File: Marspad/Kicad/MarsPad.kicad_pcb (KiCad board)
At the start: 2 copper layers, 81.5 x 83.2 mm, 30 parts, among them J1 OLED_128x64, SW1 RotaryEncoder_Switch, SW2 RotaryEncoder_Switch, U2 RP2040_Zero

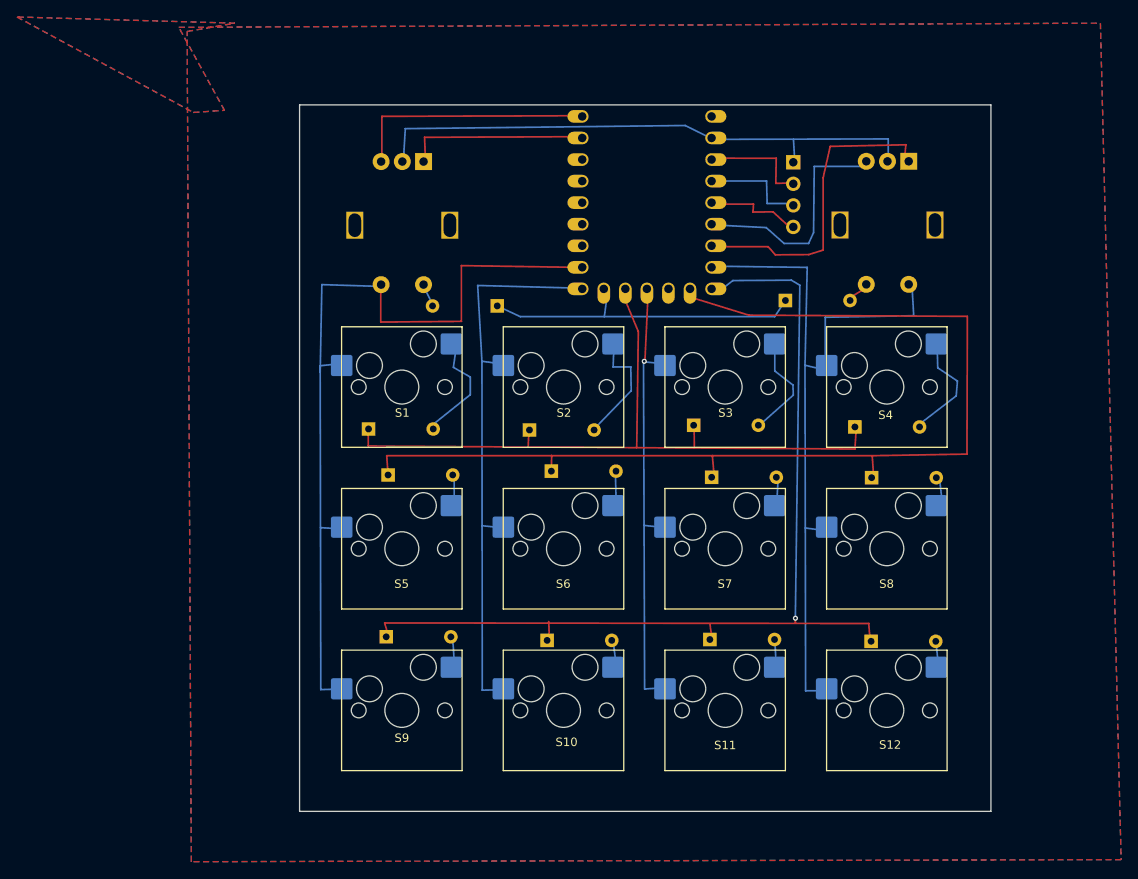
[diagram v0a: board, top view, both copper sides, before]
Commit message: added header for WS2812 led strips
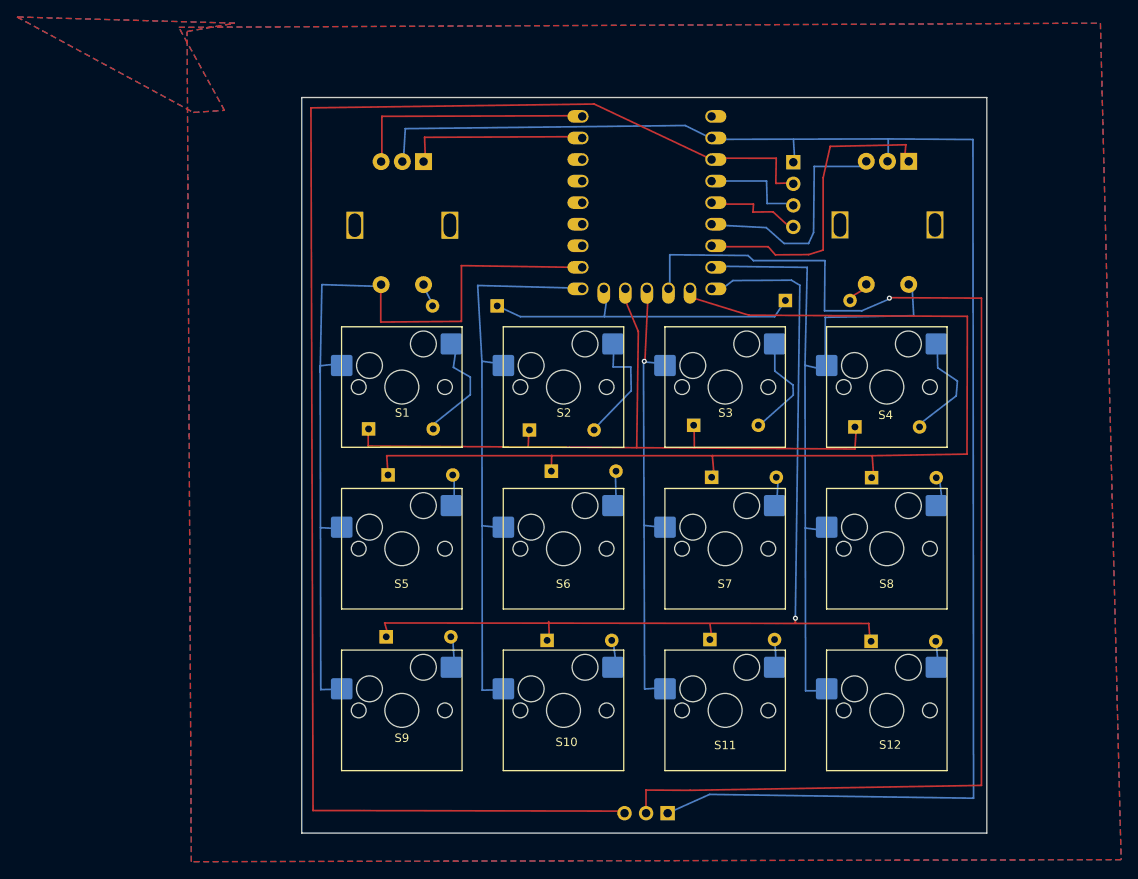
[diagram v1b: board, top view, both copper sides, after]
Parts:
- added WS2812 Header: Conn_01x03, Connector_PinSocket_2.54mm:PinSocket_1x03_P2.54mm_Vertical, B.Cu at (141.8, 126.1)
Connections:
- U2 pad 13: unconnected-(U2-12-Pad13) -> RGB
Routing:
- net RGB: vias 0 -> 1
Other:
- board size 81.5 x 83.2 mm -> 80.7 x 86.7 mm

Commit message: added RGB headers for WS2812 LEDs and fixed other artifacts.
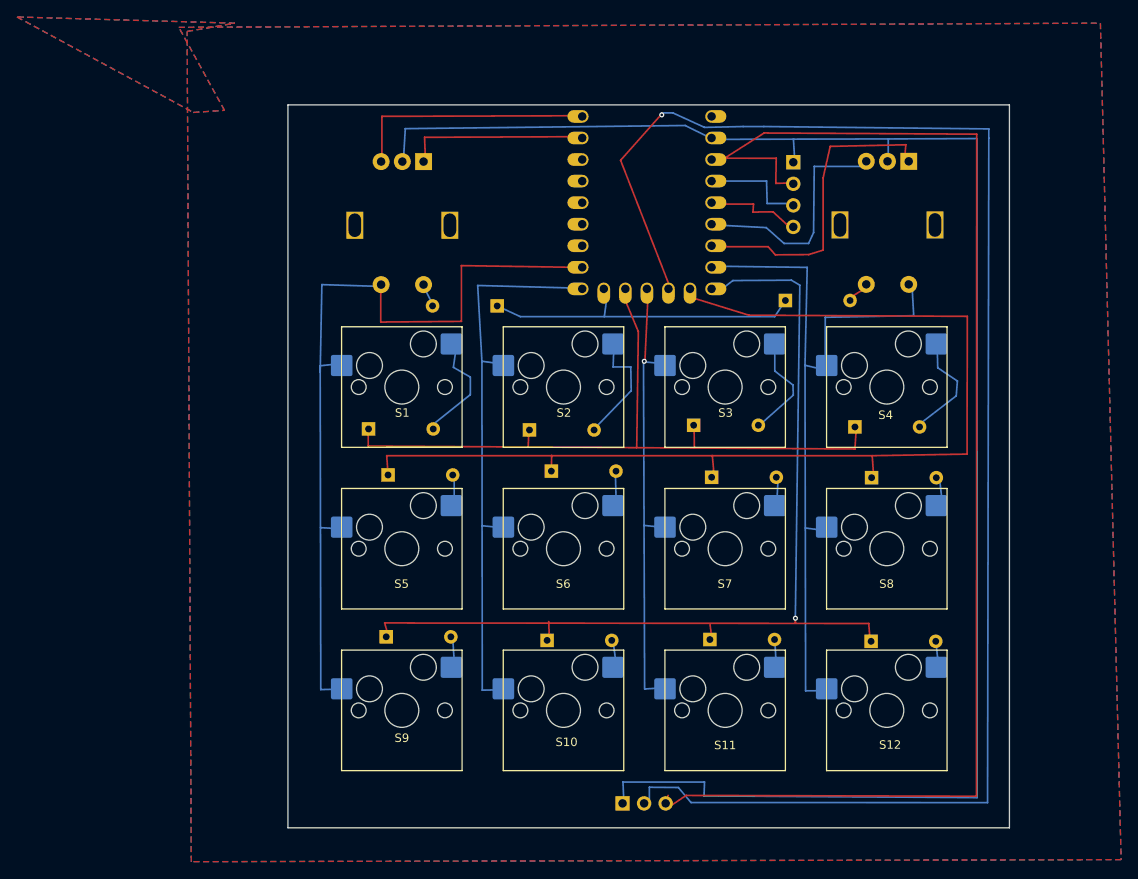
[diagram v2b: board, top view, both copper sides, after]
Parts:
- removed WS2812 Header: Conn_01x03, Connector_PinSocket_2.54mm:PinSocket_1x03_P2.54mm_Vertical
- added J2: Conn_01x03_Pin, Connector_PinSocket_2.54mm:PinSocket_1x03_P2.54mm_Vertical, B.Cu at (136.4, 125.0)
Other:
- board size 80.7 x 86.7 mm -> 85 x 85.2 mm
